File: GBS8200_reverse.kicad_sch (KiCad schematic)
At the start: 67 parts, among them IC2 74HC125, IC4 PI5C3257, IC5 1117C 1.8, P10 DE15F, P4 DE15F, P5 1x4M, 2,54 mm, P6 1x4M, 2,54 mm, P7 Cyl. 5,5x2,? mm, P8 1x2M, 2,54mm, SW1 DOWN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

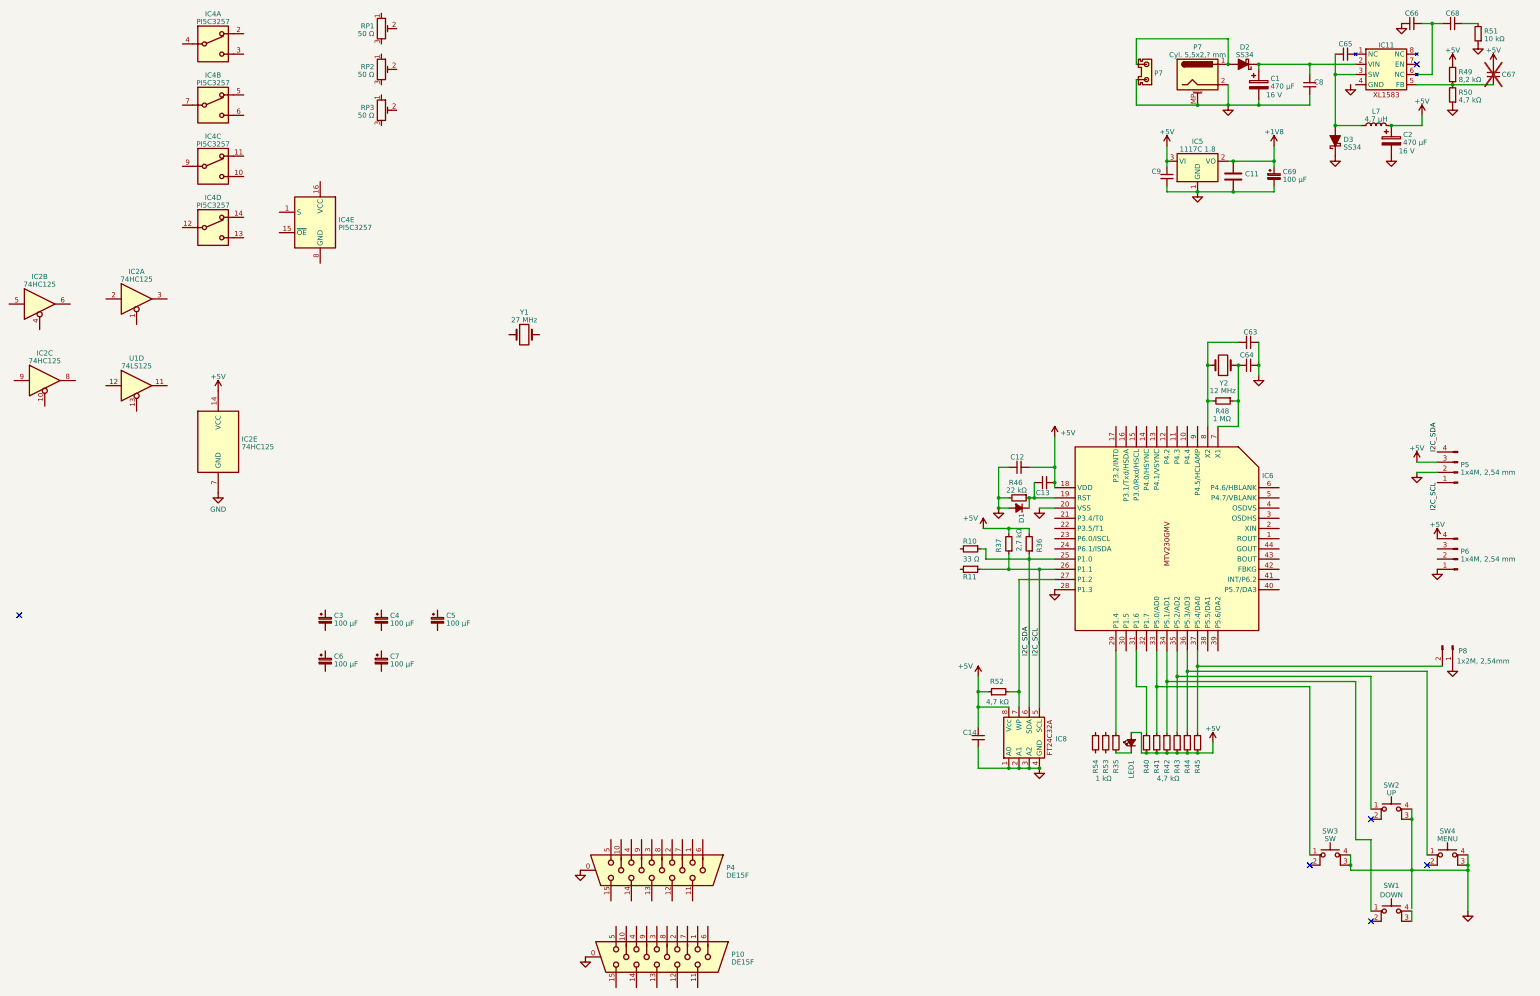
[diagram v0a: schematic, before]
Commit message: Added SDRAM and video in/out connectors
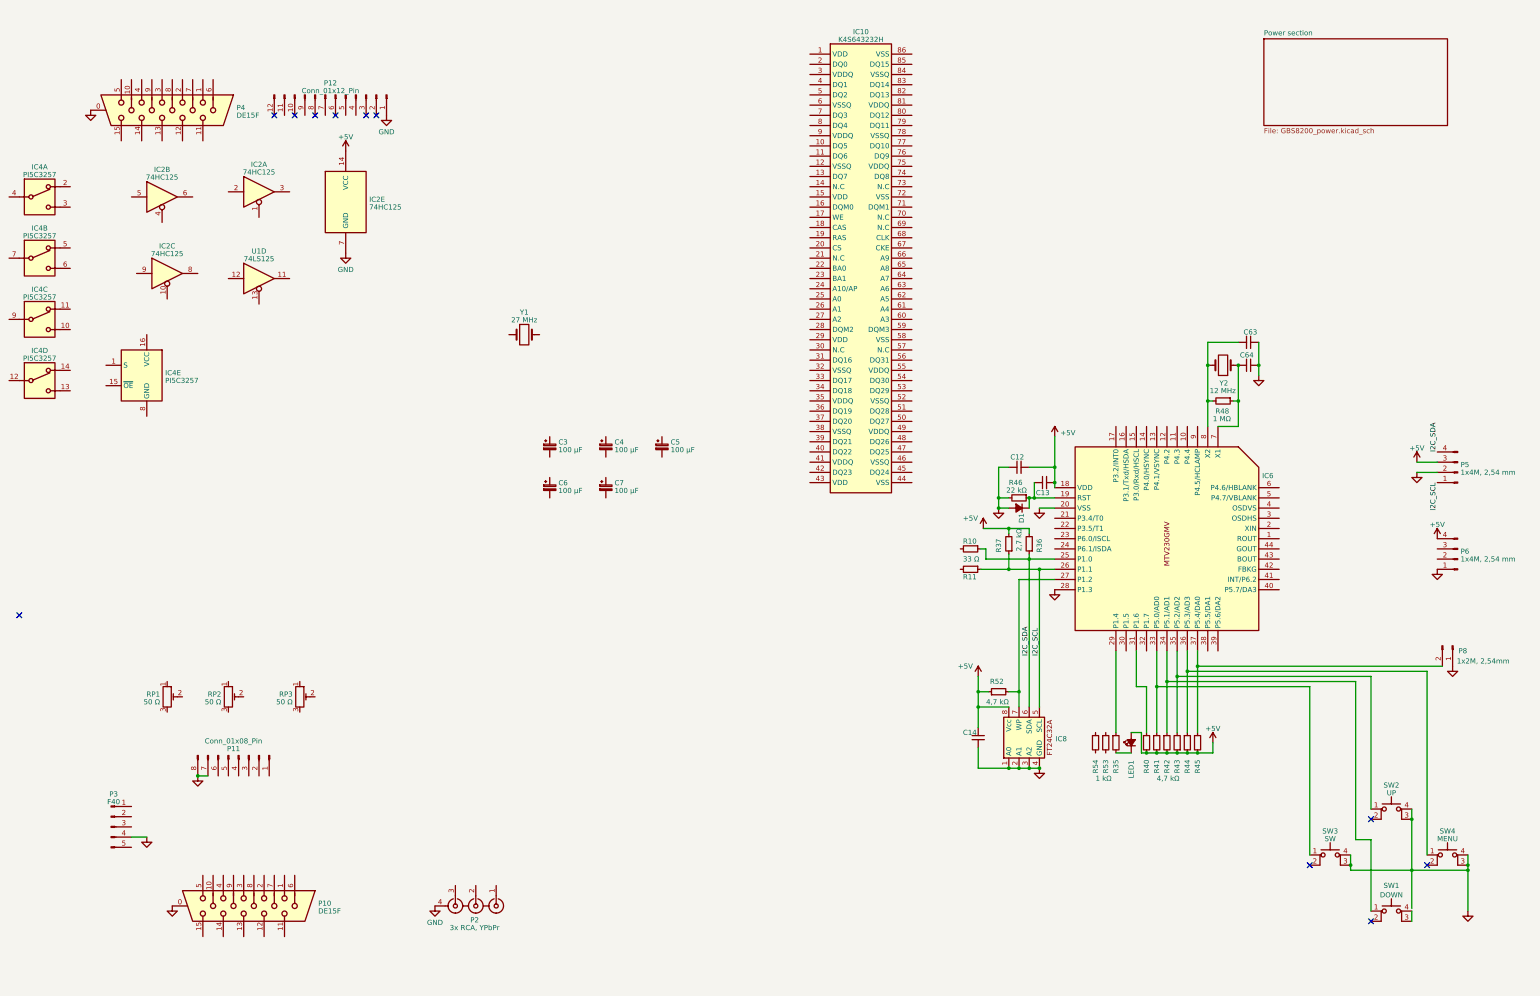
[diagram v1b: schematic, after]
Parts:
- removed C1, C2: 470 μF, symbol Device:C_Polarized
- removed C11: ~, symbol Device:C
- removed C65, C66, C67, C68, C8, C9: ~, symbol Device:C_Small
- removed C69: 100 μF, symbol Device:C_Polarized_Small
- removed D2, D3: SS34, symbol Device:D_Schottky_Filled
- removed IC11: ~, symbol GBS8200:XL1583
- removed IC5: 1117C 1.8, Package_TO_SOT_SMD:SOT-223-3_TabPin2, symbol Regulator_Linear:AMS1117-1.8
- removed L7: 4,7 μH, symbol Device:L
- removed P7: Cyl. 5,5x2,? mm, symbol Connector:Barrel_Jack_MountingPin
- removed P7: ~, symbol GBS8200:Conn_1x2_2,54mm
- removed R49: 8,2 kΩ, symbol Device:R_Small
- removed R50: 4,7 kΩ, symbol Device:R_Small
- removed R51: 10 kΩ, symbol Device:R_Small
- added IC10: K4S643232H, symbol GBS8200:K4S643232H
- added P11: Conn_01x08_Pin, symbol Connector:Conn_01x08_Pin
- added P12: Conn_01x12_Pin, symbol Connector:Conn_01x12_Pin
- added P2: 3x RCA, YPbPr, symbol GBS8200:2xRCA_YPbPr
- added P3: F40, symbol Connector:Conn_01x05_Pin
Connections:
- net GND: now also P11.7 (Pin_7), P11.8 (Pin_8), P12.1 (Pin_1), P2.4, P3.4 (Pin_4)
- no-connect marks 6 -> 11
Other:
- added sheet Power section (GBS8200_power.kicad_sch)
- moved on the sheet: C3, C4, C5, C6, C7, IC2A, IC2B, IC2C, IC2E, IC4A, IC4B, IC4C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
